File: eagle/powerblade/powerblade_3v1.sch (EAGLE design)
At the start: 91 parts, among them J1 JTAG_14PIN_IDC, J21 AC_INTBFILM, J4 TC2030-JLINK-NL, Q1 2N7002, Q3 2SK1829, Q4 2SK1829, U1 TPS62122, U2 MCP6V3, U3 MSP430FR5738, U4 NRF51822QF, U6 MAX9910, U7 OPA2369, X1 16MHz, X2 ABS05-32.768KHZ-9-T, X3 32.768kHz

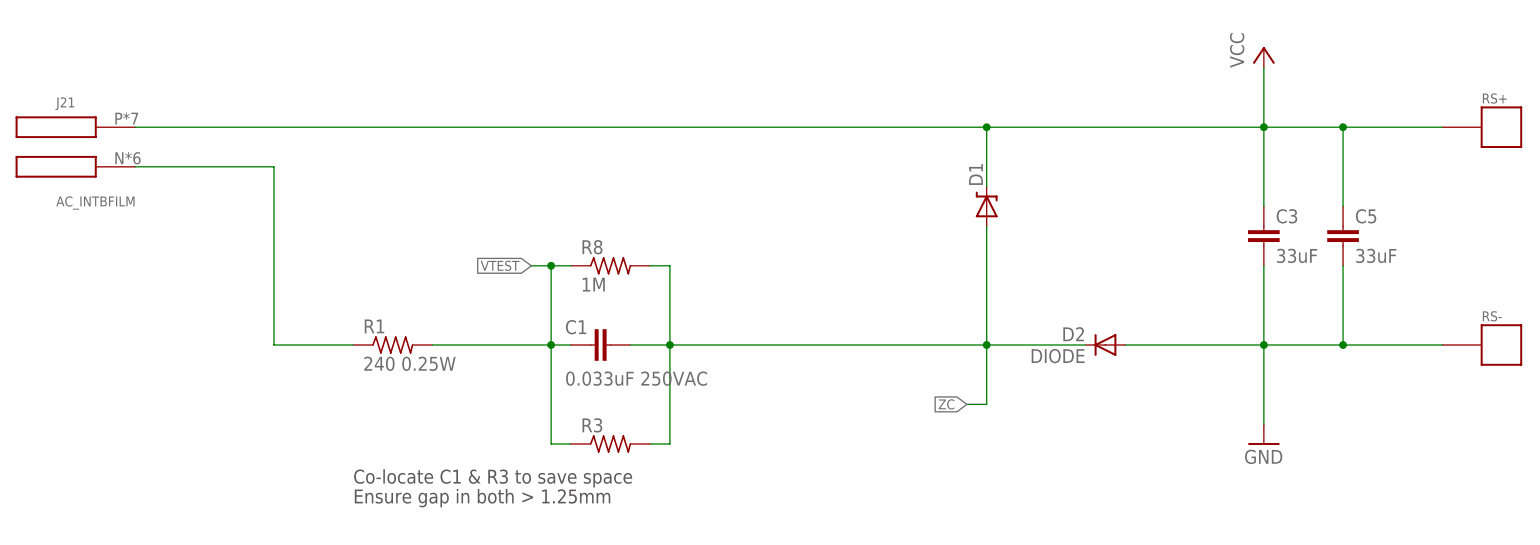
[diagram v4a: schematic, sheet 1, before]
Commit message: finished parts for first page
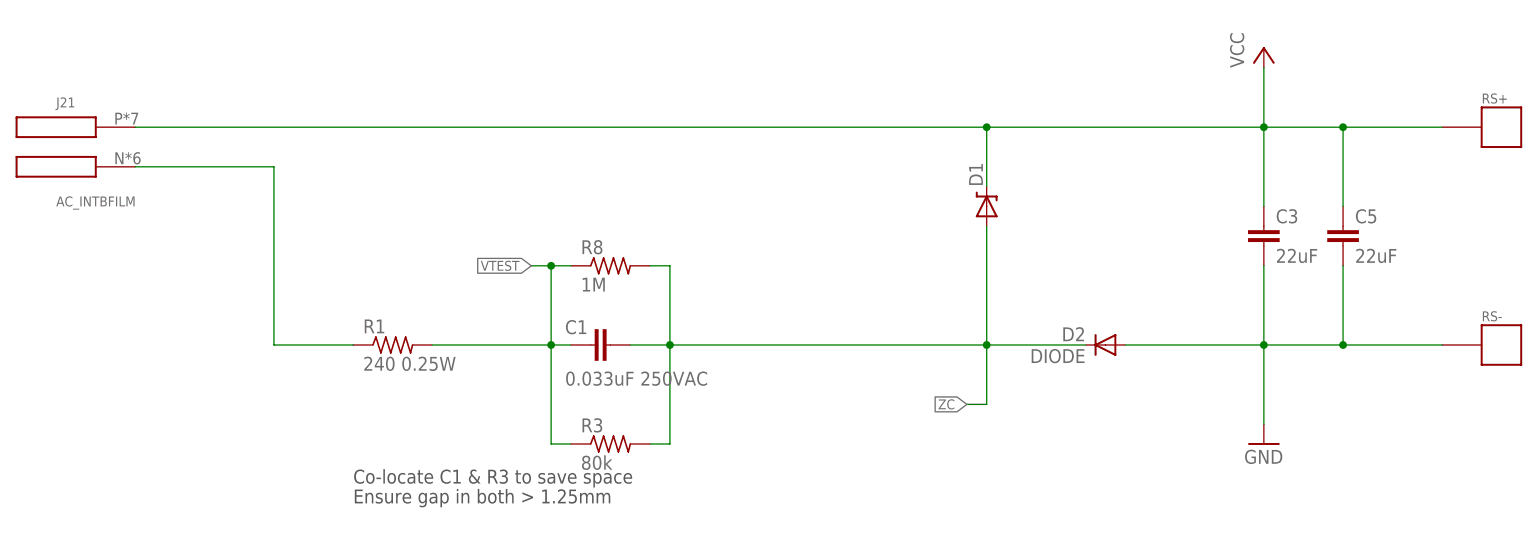
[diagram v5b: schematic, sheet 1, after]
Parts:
- C10: DIGIKEY (none) -> 445-9077-1-ND
- C3, C5: value 33uF -> 22uF; DIGIKEY 718-1672-1-ND -> 445-9077-1-ND
- D1: DIGIKEY_2 BZT52C15T-7DICT-ND -> (none)
- R3: value (none) -> 80k; DIGIKEY (none) -> P80.6KAACT-ND; DIGIKEY_2 (none) -> P69.8KAACT-ND; DIGIKEY_3 (none) -> P40.2KAACT-ND
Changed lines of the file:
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@@
 <part name="D1" library="powerfilm" deviceset="ZENER" device="BZT52">
 <attribute name="DIGIKEY" value="BZT52C10T-7DICT-ND "/>
-<attribute name="DIGIKEY_2" value="BZT52C15T-7DICT-ND "/>
 </part>
 <part name="D2" library="powerfilm" deviceset="DIODE" device=""/>
-<part name="C3" library="rcl" deviceset="C-EU" device="C0603" value="33uF">
-<attribute name="DIGIKEY" value="718-1672-1-ND"/>
+<part name="C3" library="rcl" deviceset="C-EU" device="C0603" value="22uF">
+<attribute name="DIGIKEY" value="445-9077-1-ND"/>
 </part>
 <part name="GND1" library="supply1" deviceset="GND" device=""/>
@@
 <part name="C8" library="rcl" deviceset="C-EU" device="C0402" value="0.1uF"/>
 <part name="C9" library="rcl" deviceset="C-EU" device="C0402" value="0.1uF"/>
-<part name="C10" library="rcl" deviceset="C-EU" device="C0603" value="22uF"/>
+<part name="C10" library="rcl" deviceset="C-EU" device="C0603" value="22uF">
+<attribute name="DIGIKEY" value="445-9077-1-ND"/>
+</part>
 <part name="GND6" library="supply1" deviceset="GND" device=""/>
 <part name="GND7" library="supply1" deviceset="GND" device=""/>
@@
 <part name="C2" library="rcl" deviceset="C-EU" device="C0603"/>
 <part name="U2" library="powerfilm" deviceset="MCP6V3" device=""/>
-<part name="R3" library="rcl" deviceset="R-US_" device="R1210"/>
-<part name="C5" library="rcl" deviceset="C-EU" device="C0603" value="33uF">
-<attribute name="DIGIKEY" value="718-1672-1-ND"/>
+<part name="R3" library="rcl" deviceset="R-US_" device="R1210" value="80k">
+<attribute name="DIGIKEY" value="P80.6KAACT-ND"/>
+<attribute name="DIGIKEY_2" value="P69.8KAACT-ND"/>
+<attribute name="DIGIKEY_3" value="P40.2KAACT-ND"/>
+</part>
+<part name="C5" library="rcl" deviceset="C-EU" device="C0603" value="22uF">
+<attribute name="DIGIKEY" value="445-9077-1-ND"/>
 </part>
 <part name="U3" library="powerfilm" deviceset="MSP430FR5738" device=""/>
@@
 <instance part="D1" gate="G$1" x="58.42" y="7.62" smashed="yes" rot="R90">
 <attribute name="NAME" x="57.9374" y="10.16" size="1.778" layer="95" rot="R90"/>
-<attribute name="DIGIKEY_2" x="58.42" y="7.62" size="1.778" layer="96" rot="R90" display="off"/>
 </instance>
 <instance part="D2" gate="G$1" x="73.66" y="-10.16" rot="MR0"/>
@@
 <attribute name="DIGIKEY" x="10.16" y="0" size="1.778" layer="96" display="off"/>
 </instance>
-<instance part="R3" gate="G$1" x="10.16" y="-22.86"/>
+<instance part="R3" gate="G$1" x="10.16" y="-22.86">
+<attribute name="DIGIKEY" x="10.16" y="-22.86" size="1.27" layer="96" display="off"/>
+<attribute name="DIGIKEY_2" x="10.16" y="-22.86" size="1.27" layer="96" display="off"/>
+<attribute name="DIGIKEY_3" x="10.16" y="-22.86" size="1.27" layer="96" display="off"/>
+</instance>
 <instance part="C5" gate="G$1" x="104.14" y="5.08">
 <attribute name="DIGIKEY" x="104.14" y="5.08" size="1.778" layer="96" display="off"/>
@@
 <instance part="C8" gate="G$1" x="-40.64" y="0"/>
 <instance part="C9" gate="G$1" x="53.34" y="0"/>
-<instance part="C10" gate="G$1" x="63.5" y="0"/>
+<instance part="C10" gate="G$1" x="63.5" y="0">
+<attribute name="DIGIKEY" x="63.5" y="0" size="1.27" layer="96" display="off"/>
+</instance>
 <instance part="GND6" gate="1" x="-40.64" y="-30.48"/>
 <instance part="GND7" gate="1" x="63.5" y="-30.48"/>

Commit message: finished parts
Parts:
- R11, R22: value 134k 1% -> 670k; DIGIKEY P133KHCT-ND -> (none)
- R12, R13: value 67k 1% -> 330k; DIGIKEY P66.5KHCT-ND -> (none)
- R15: value NP -> 1M 1%; DIGIKEY NP -> (none)
- R16: value 0 -> 75 1%; DIGIKEY P0.0JCT-ND -> (none)
- R18: value 2.49 1% -> 4.99 1%
- R20, R21: DIGIKEY P10.0KLCT-ND -> (none)
- R35: value 2k 1% -> 20k
- R37: value 90k 1% -> 887k 1%
- R38: value 3.1k 1% -> 137k 1%
- R39: value 100k 1% -> 71.5k 1%
- R40: value 100k 1% -> 1M 1%; DIGIKEY P100KLCT-ND -> (none)
- R6: value 220k -> 660k
- RF: value 1.5k 1% -> 4.99k 1%; DIGIKEY P1.50KLCT-ND -> (none)
- RI1, RI2: value 220k 1% -> 953k 1%; DIGIKEY P220KLCT-ND -> (none)
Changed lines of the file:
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@@
 <attribute name="DIGIKEY" value="P200LCT-ND"/>
 </part>
-<part name="R15" library="rcl" deviceset="R-US_" device="R0402" value="NP">
-<attribute name="DIGIKEY" value="NP"/>
-</part>
-<part name="R16" library="rcl" deviceset="R-US_" device="R0402" value="0">
-<attribute name="DIGIKEY" value="P0.0JCT-ND"/>
-</part>
+<part name="R15" library="rcl" deviceset="R-US_" device="R0402" value="1M 1%"/>
+<part name="R16" library="rcl" deviceset="R-US_" device="R0402" value="75 1%"/>
 <part name="R17" library="rcl" deviceset="R-US_" device="R0402" value="20k 1%">
 <attribute name="DIGIKEY" value="P20.0KLCT-ND"/>
 </part>
-<part name="R18" library="rcl" deviceset="R-US_" device="R0402" value="2.49 1%">
+<part name="R18" library="rcl" deviceset="R-US_" device="R0402" value="4.99 1%">
 <attribute name="DIGIKEY" value="541-2.49LLCT-ND"/>
 </part>
@@
 <attribute name="DIGIKEY" value="445-1265-1-ND"/>
 </part>
-<part name="RF" library="rcl" deviceset="R-US_" device="R0402" value="1.5k 1%">
-<attribute name="DIGIKEY" value="P1.50KLCT-ND"/>
-</part>
-<part name="R20" library="rcl" deviceset="R-US_" device="R0402" value="1M 1%">
-<attribute name="DIGIKEY" value="P10.0KLCT-ND"/>
-</part>
-<part name="R21" library="rcl" deviceset="R-US_" device="R0402" value="1M 1%">
-<attribute name="DIGIKEY" value="P10.0KLCT-ND"/>
-</part>
-<part name="RI1" library="rcl" deviceset="R-US_" device="R0402" value="220k 1%">
-<attribute name="DIGIKEY" value="P220KLCT-ND"/>
-</part>
-<part name="RI2" library="rcl" deviceset="R-US_" device="R0402" value="220k 1%">
-<attribute name="DIGIKEY" value="P220KLCT-ND"/>
-</part>
+<part name="RF" library="rcl" deviceset="R-US_" device="R0402" value="4.99k 1%"/>
+<part name="R20" library="rcl" deviceset="R-US_" device="R0402" value="1M 1%"/>
+<part name="R21" library="rcl" deviceset="R-US_" device="R0402" value="1M 1%"/>
+<part name="RI1" library="rcl" deviceset="R-US_" device="R0402" value="953k 1%"/>
+<part name="RI2" library="rcl" deviceset="R-US_" device="R0402" value="953k 1%"/>
 <part name="+3V5" library="supply1" deviceset="+3V3" device=""/>
 <part name="+3V6" library="supply1" deviceset="+3V3" device=""/>
@@
 </part>
 <part name="+3V3" library="supply1" deviceset="+3V3" device=""/>
-<part name="R35" library="rcl" deviceset="R-US_" device="R0402" value="2k 1%">
+<part name="R35" library="rcl" deviceset="R-US_" device="R0402" value="20k">
 <attribute name="DIGIKEY" value="P2.00KLCT-ND"/>
 </part>
-<part name="R37" library="rcl" deviceset="R-US_" device="R0402" value="90k 1%">
+<part name="R37" library="rcl" deviceset="R-US_" device="R0402" value="887k 1%">
 <attribute name="DIGIKEY" value="P90.9KLCT-ND"/>
 </part>
-<part name="R38" library="rcl" deviceset="R-US_" device="R0402" value="3.1k 1%">
+<part name="R38" library="rcl" deviceset="R-US_" device="R0402" value="137k 1%">
 <attribute name="DIGIKEY" value="P3.09KHCT-ND"/>
 </part>
-<part name="R40" library="rcl" deviceset="R-US_" device="R0402" value="100k 1%">
-<attribute name="DIGIKEY" value="P100KLCT-ND"/>
-</part>
+<part name="R40" library="rcl" deviceset="R-US_" device="R0402" value="1M 1%"/>
 <part name="C39" library="rcl" deviceset="C-EU" device="C0402" value="1.5uF">
 <attribute name="DIGIKEY" value="445-13874-1-ND"/>
@@
 <attribute name="DIGIKEY" value="5126K-ND"/>
 </part>
-<part name="R39" library="rcl" deviceset="R-US_" device="R0402" value="100k 1%">
+<part name="R39" library="rcl" deviceset="R-US_" device="R0402" value="71.5k 1%">
 <attribute name="DIGIKEY" value="P100KLCT-ND"/>
 </part>
@@
 <part name="+3V7" library="supply1" deviceset="+3V3" device=""/>
 <part name="GND23" library="supply1" deviceset="GND" device=""/>
-<part name="R11" library="rcl" deviceset="R-US_" device="R0603" value="134k 1%">
-<attribute name="DIGIKEY" value="P133KHCT-ND"/>
-</part>
-<part name="R12" library="rcl" deviceset="R-US_" device="R0603" value="67k 1%">
-<attribute name="DIGIKEY" value="P66.5KHCT-ND"/>
-</part>
+<part name="R11" library="rcl" deviceset="R-US_" device="R0603" value="670k"/>
+<part name="R12" library="rcl" deviceset="R-US_" device="R0603" value="330k"/>
 <part name="GND25" library="supply1" deviceset="GND" device=""/>
 <part name="P+4" library="supply1" deviceset="VCC" device=""/>
@@
 <part name="Q4" library="powerfilm" deviceset="2SK1829" device=""/>
 <part name="SUPPLY19" library="supply2" deviceset="GND3" device=""/>
-<part name="R6" library="rcl" deviceset="R-US_" device="R0603" value="220k"/>
+<part name="R6" library="rcl" deviceset="R-US_" device="R0603" value="660k"/>
 <part name="SUPPLY20" library="supply2" deviceset="GND3" device=""/>
 <part name="SUPPLY21" library="supply2" deviceset="GND3" device=""/>
@@
 <part name="GND2" library="supply1" deviceset="GND" device=""/>
 <part name="R10" library="rcl" deviceset="R-US_" device="R0603" value="220k"/>
-<part name="R13" library="rcl" deviceset="R-US_" device="R0603" value="67k 1%">
-<attribute name="DIGIKEY" value="P66.5KHCT-ND"/>
-</part>
-<part name="R22" library="rcl" deviceset="R-US_" device="R0603" value="134k 1%">
-<attribute name="DIGIKEY" value="P133KHCT-ND"/>
-</part>
+<part name="R13" library="rcl" deviceset="R-US_" device="R0603" value="330k"/>
+<part name="R22" library="rcl" deviceset="R-US_" device="R0603" value="670k"/>
 <part name="GND8" library="supply1" deviceset="GND" device=""/>
 </parts>
@@
 <instance part="+3V7" gate="G$1" x="35.56" y="66.04"/>
 <instance part="GND23" gate="1" x="-7.62" y="38.1"/>
-<instance part="R11" gate="G$1" x="78.74" y="5.08" rot="R90">
-<attribute name="DIGIKEY" x="78.74" y="5.08" size="1.27" layer="96" rot="R90" display="off"/>
-</instance>
-<instance part="R12" gate="G$1" x="78.74" y="-10.16" rot="R90">
-<attribute name="DIGIKEY" x="78.74" y="-10.16" size="1.27" layer="96" rot="R90" display="off"/>
-</instance>
+<instance part="R11" gate="G$1" x="78.74" y="5.08" rot="R90"/>
+<instance part="R12" gate="G$1" x="78.74" y="-10.16" rot="R90"/>
 <instance part="GND25" gate="1" x="78.74" y="-20.32"/>
 <instance part="P+4" gate="VCC" x="78.74" y="15.24"/>
@@
 <instance part="GND27" gate="1" x="71.12" y="30.48"/>
 <instance part="R10" gate="G$1" x="63.5" y="35.56"/>
-<instance part="R13" gate="G$1" x="60.96" y="2.54" rot="R90">
-<attribute name="DIGIKEY" x="60.96" y="2.54" size="1.27" layer="96" rot="R90" display="off"/>
-</instance>
-<instance part="R22" gate="G$1" x="60.96" y="17.78" rot="R90">
-<attribute name="DIGIKEY" x="60.96" y="17.78" size="1.27" layer="96" rot="R90" display="off"/>
-</instance>
+<instance part="R13" gate="G$1" x="60.96" y="2.54" rot="R90"/>
+<instance part="R22" gate="G$1" x="60.96" y="17.78" rot="R90"/>
 <instance part="GND8" gate="1" x="60.96" y="-7.62"/>
 </instances>
@@
 <attribute name="DIGIKEY" x="68.58" y="-17.78" size="1.27" layer="96" rot="R90" display="off"/>
 </instance>
-<instance part="R15" gate="G$1" x="43.18" y="-30.48">
-<attribute name="DIGIKEY" x="43.18" y="-30.48" size="1.27" layer="96" display="off"/>
-</instance>
-<instance part="R16" gate="G$1" x="50.8" y="-38.1" rot="R90">
-<attribute name="DIGIKEY" x="50.8" y="-38.1" size="1.27" layer="96" rot="R90" display="off"/>
-</instance>
+<instance part="R15" gate="G$1" x="43.18" y="-30.48"/>
+<instance part="R16" gate="G$1" x="50.8" y="-38.1" rot="R90"/>
 <instance part="R17" gate="G$1" x="93.98" y="-30.48">
 <attribute name="DIGIKEY" x="93.98" y="-30.48" size="1.27" layer="96" display="off"/>
@@
 <attribute name="DIGIKEY" x="-20.32" y="5.08" size="1.27" layer="96" display="off"/>
 </instance>
-<instance part="RF" gate="G$1" x="-30.48" y="-35.56">
-<attribute name="DIGIKEY" x="-30.48" y="-35.56" size="1.27" layer="96" display="off"/>
-</instance>
-<instance part="R20" gate="G$1" x="-35.56" y="10.16">
-<attribute name="DIGIKEY" x="-35.56" y="10.16" size="1.27" layer="96" display="off"/>
-</instance>
-<instance part="R21" gate="G$1" x="-50.8" y="10.16">
-<attribute name="DIGIKEY" x="-50.8" y="10.16" size="1.27" layer="96" display="off"/>
-</instance>
-<instance part="RI1" gate="G$1" x="-50.8" y="-15.24">
-<attribute name="DIGIKEY" x="-50.8" y="-15.24" size="1.27" layer="96" display="off"/>
-</instance>
-<instance part="RI2" gate="G$1" x="-50.8" y="-35.56">
-<attribute name="DIGIKEY" x="-50.8" y="-35.56" size="1.27" layer="96" display="off"/>
-</instance>
+<instance part="RF" gate="G$1" x="-30.48" y="-35.56"/>
+<instance part="R20" gate="G$1" x="-35.56" y="10.16"/>
+<instance part="R21" gate="G$1" x="-50.8" y="10.16"/>
+<instance part="RI1" gate="G$1" x="-50.8" y="-15.24"/>
+<instance part="RI2" gate="G$1" x="-50.8" y="-35.56"/>
 <instance part="+3V5" gate="G$1" x="-27.94" y="17.78"/>
 <instance part="+3V6" gate="G$1" x="93.98" y="20.32"/>
@@
 <attribute name="DIGIKEY" x="160.02" y="-38.1" size="1.27" layer="96" rot="R90" display="off"/>
 </instance>
-<instance part="R40" gate="G$1" x="116.84" y="27.94" rot="R90">
-<attribute name="DIGIKEY" x="116.84" y="27.94" size="1.27" layer="96" rot="R90" display="off"/>
-</instance>
+<instance part="R40" gate="G$1" x="116.84" y="27.94" rot="R90"/>
 <instance part="C39" gate="G$1" x="142.24" y="-10.16" rot="R90">
 <attribute name="DIGIKEY" x="142.24" y="-10.16" size="1.27" layer="96" rot="R90" display="off"/>

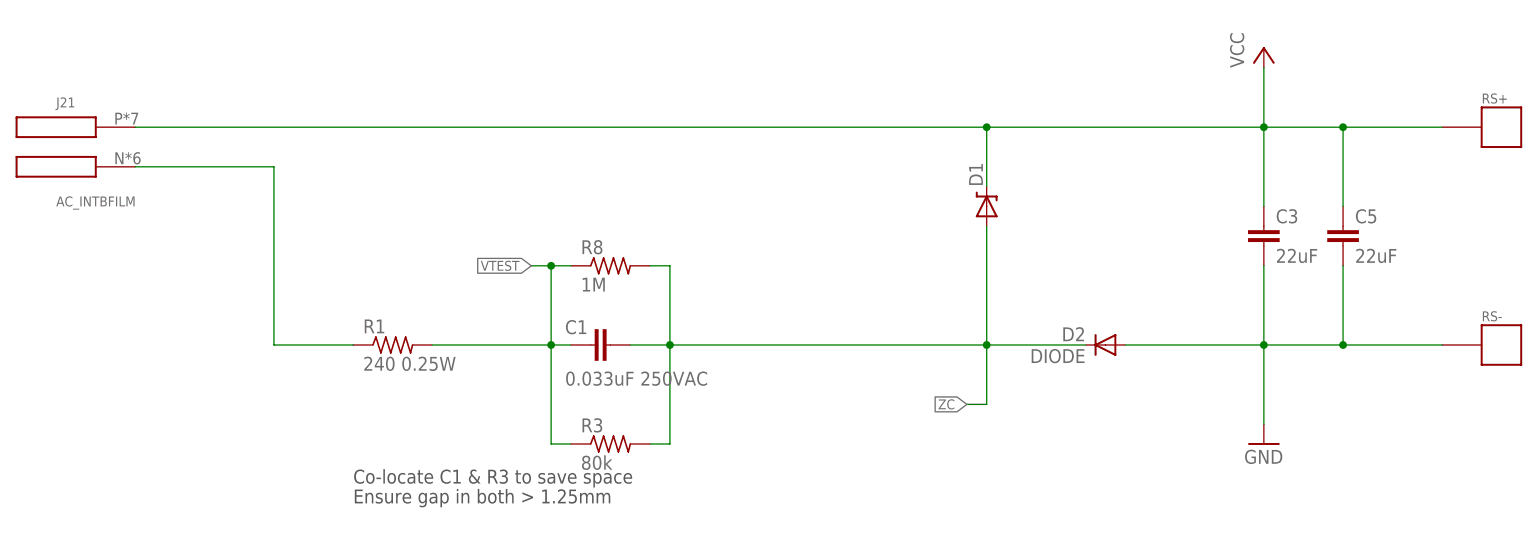
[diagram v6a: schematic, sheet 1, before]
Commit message: post mortem changes to schematic
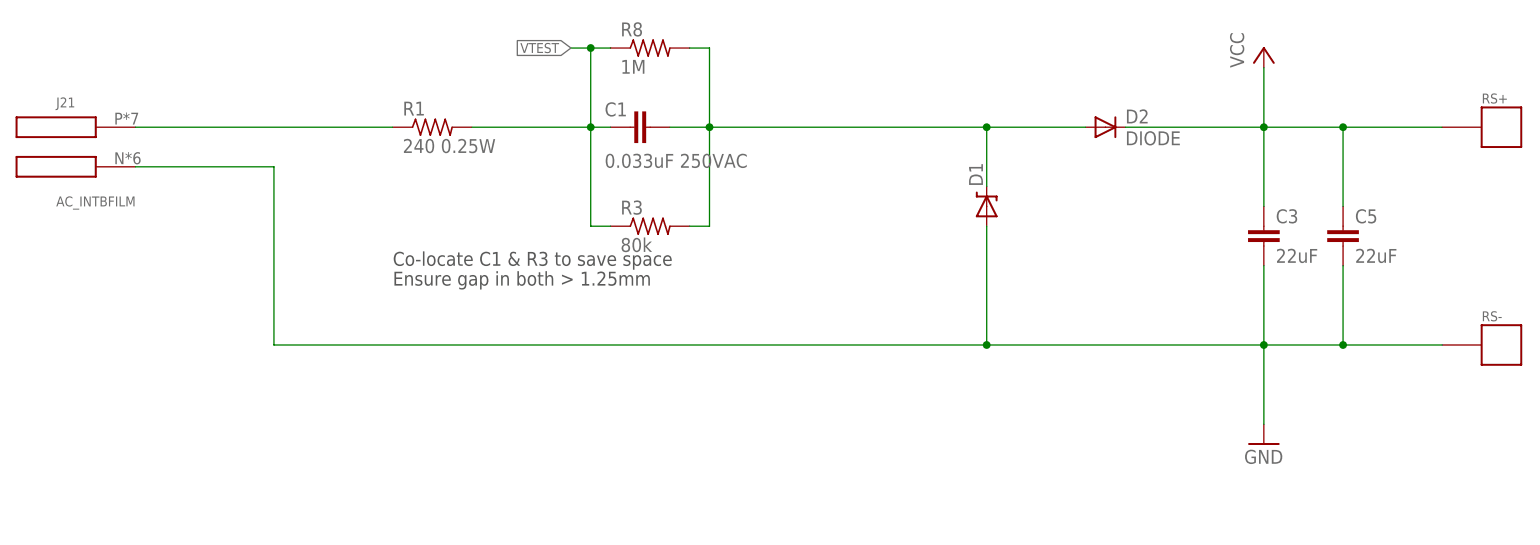
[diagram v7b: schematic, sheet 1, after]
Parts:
- added R24: 1 1%, rcl:R-US_R0603
- added VS-: TP_LONG, skyspecs:TP_LONG
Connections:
- new net N$12: J21.P, R1.1
- new net N$7: C10.1, C4.1, C9.1, L1.1, R24.1, R7.2, U1.VOUT, VS+.P$1
- new net PWM_CURRENT: U3.P1.2/TA1.1/A2
- new net PWM_VOLTAGE: U3.P1.3/TA1.2/A3
- net +3V3: now also R24.2, VS-.P$1; no longer C10.1, C4.1, C9.1, L1.1, R7.2, U1.VOUT, VS+.P$1
- net GND: now also D1.A, J21.N; no longer D2.A
- net N$2: now also C1.1, D1.C, D2.A, R3.2, R8.2; no longer J21.N, R1.1
- net N$8: now also U3.P1.0/VREF-; no longer U3.P1.2/TA1.1/A2
- net VCC: now also D2.C; no longer D1.C, J21.P
- net VCC_SENSE: now also U3.P1.1/VREF+; no longer U3.P1.3/TA1.2/A3
- net ZC: no longer C1.1, D1.A, D2.C, R3.2, R8.2
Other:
- moved on the sheet: C1, D2, R1, R3, R8, VS+
